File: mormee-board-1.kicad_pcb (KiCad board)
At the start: 2 copper layers, 1 part, among them U1 RTL8735BDM-A20-N04

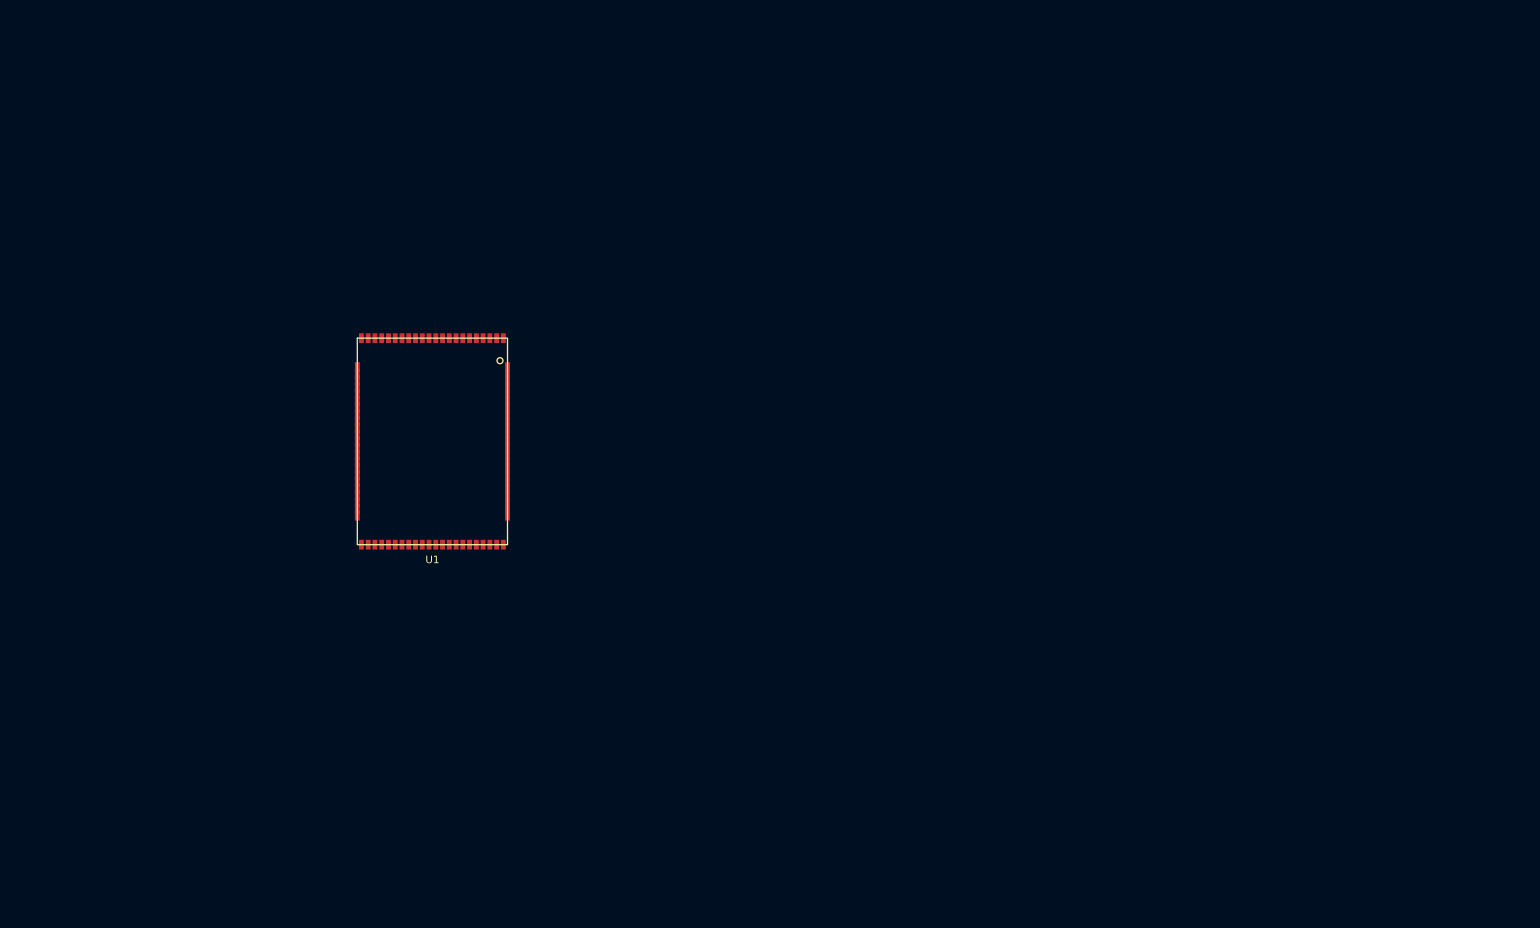
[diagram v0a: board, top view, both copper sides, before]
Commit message: All footprints configured correctly. Next step is layout
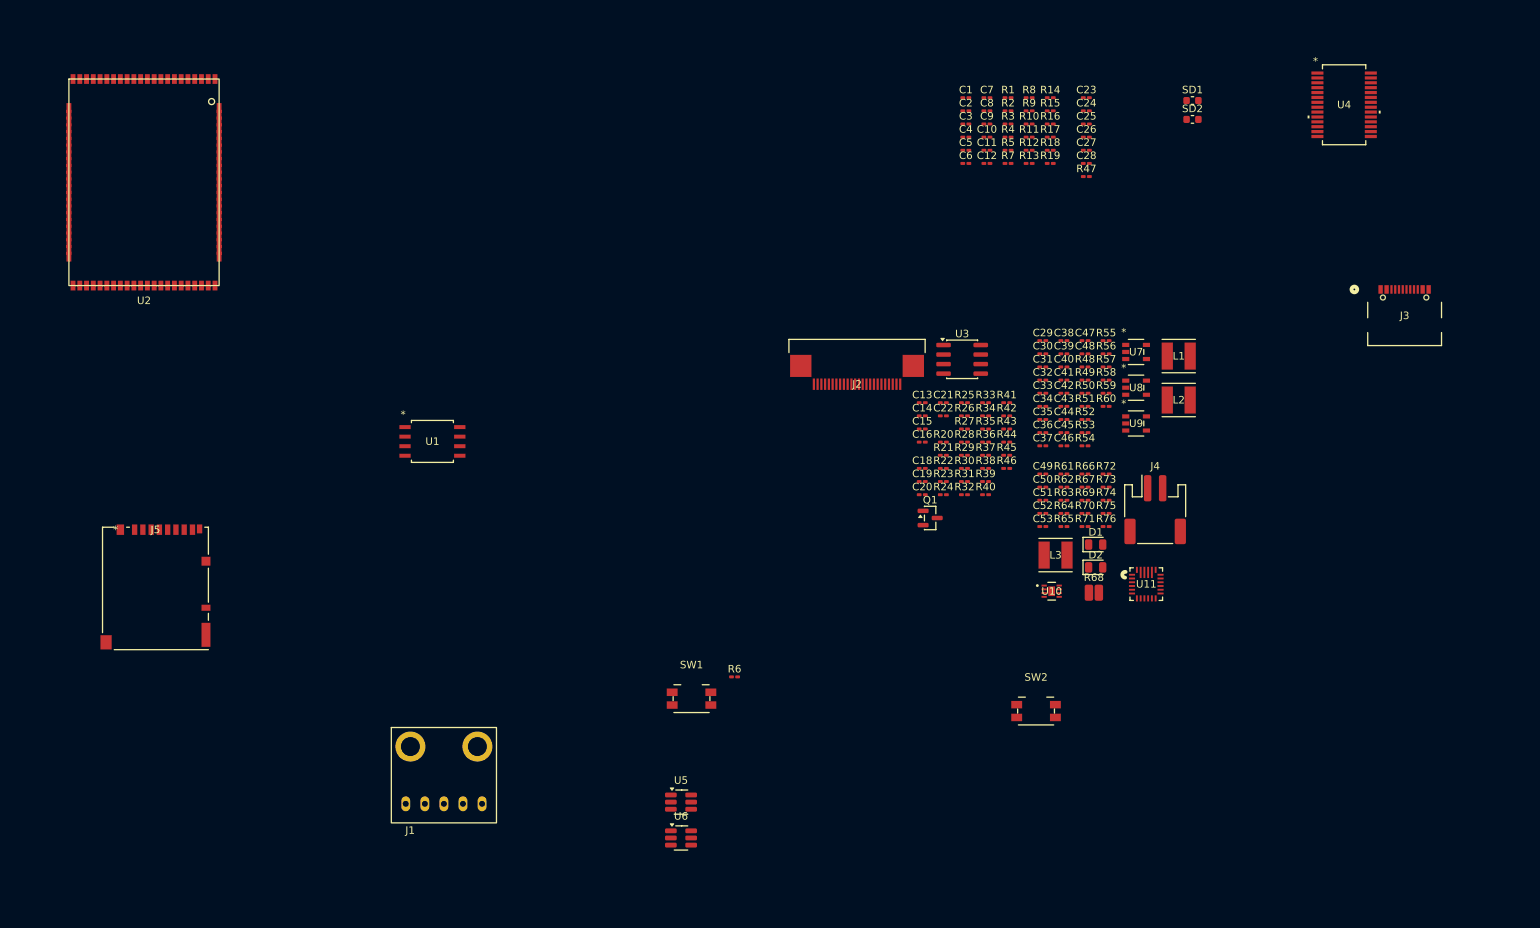
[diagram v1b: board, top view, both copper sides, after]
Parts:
- added C1: 0.1uF/10V, Capacitor_SMD:C_0201_0603Metric_Pad0.64x0.40mm_HandSolder, F.Cu at (193.6, 32.5)
- added C10: 4.7uF/10V, Capacitor_SMD:C_0201_0603Metric_Pad0.64x0.40mm_HandSolder, F.Cu at (196.4, 37.7)
- added C11: 0.1uF/10V, Capacitor_SMD:C_0201_0603Metric_Pad0.64x0.40mm_HandSolder, F.Cu at (196.4, 39.5)
- added C12: 10uF/10V, Capacitor_SMD:C_0201_0603Metric_Pad0.64x0.40mm_HandSolder, F.Cu at (196.4, 41.2)
- added C13: 0.1uF/10V, Capacitor_SMD:C_0201_0603Metric_Pad0.64x0.40mm_HandSolder, F.Cu at (187.8, 73.1)
- added C14: 2.2uF/10V, Capacitor_SMD:C_0201_0603Metric_Pad0.64x0.40mm_HandSolder, F.Cu at (187.8, 74.8)
- added C15: 10uF/10V, Capacitor_SMD:C_0201_0603Metric_Pad0.64x0.40mm_HandSolder, F.Cu at (187.8, 76.6)
- added C16: 0.1uF/10V, Capacitor_SMD:C_0201_0603Metric_Pad0.64x0.40mm_HandSolder, F.Cu at (187.8, 78.3)
- added C18: 0.1uF/10V, Capacitor_SMD:C_0201_0603Metric_Pad0.64x0.40mm_HandSolder, F.Cu at (187.8, 81.8)
- added C19: 0.1uF/10V, Capacitor_SMD:C_0201_0603Metric_Pad0.64x0.40mm_HandSolder, F.Cu at (187.8, 83.6)
- added C2: 0.1uF/10V, Capacitor_SMD:C_0201_0603Metric_Pad0.64x0.40mm_HandSolder, F.Cu at (193.6, 34.2)
- added C20: 0.1uF/10V, Capacitor_SMD:C_0201_0603Metric_Pad0.64x0.40mm_HandSolder, F.Cu at (187.8, 85.3)
- added C21: 0.1uF/10V/NC, Capacitor_SMD:C_0201_0603Metric_Pad0.64x0.40mm_HandSolder, F.Cu at (190.6, 73.1)
- added C22: 0.1uF/10V, Capacitor_SMD:C_0201_0603Metric_Pad0.64x0.40mm_HandSolder, F.Cu at (190.6, 74.8)
- added C23: 0.1uF/10V, Capacitor_SMD:C_0201_0603Metric_Pad0.64x0.40mm_HandSolder, F.Cu at (209.6, 32.5)
- added C24: 2.2uF/10V, Capacitor_SMD:C_0201_0603Metric_Pad0.64x0.40mm_HandSolder, F.Cu at (209.6, 34.2)
- added C25: 0.1uF, Capacitor_SMD:C_0201_0603Metric_Pad0.64x0.40mm_HandSolder, F.Cu at (209.6, 36.0)
- added C26: 0.1uF, Capacitor_SMD:C_0201_0603Metric_Pad0.64x0.40mm_HandSolder, F.Cu at (209.6, 37.7)
- added C27: 0.1uF, Capacitor_SMD:C_0201_0603Metric_Pad0.64x0.40mm_HandSolder, F.Cu at (209.6, 39.5)
- added C28: 4.7uF, Capacitor_SMD:C_0201_0603Metric_Pad0.64x0.40mm_HandSolder, F.Cu at (209.6, 41.2)
- added C29: 0.1uF/10V, Capacitor_SMD:C_0201_0603Metric_Pad0.64x0.40mm_HandSolder, F.Cu at (203.8, 64.8)
- added C3: 10uF/10V, Capacitor_SMD:C_0201_0603Metric_Pad0.64x0.40mm_HandSolder, F.Cu at (193.6, 36.0)
- added C30: 0.1uF/10V, Capacitor_SMD:C_0201_0603Metric_Pad0.64x0.40mm_HandSolder, F.Cu at (203.8, 66.6)
- added C31: 10uF/10V, Capacitor_SMD:C_0201_0603Metric_Pad0.64x0.40mm_HandSolder, F.Cu at (203.8, 68.3)
- added C32: 10uF/10V, Capacitor_SMD:C_0201_0603Metric_Pad0.64x0.40mm_HandSolder, F.Cu at (203.8, 70.1)
- added C33: 68pF, Capacitor_SMD:C_0201_0603Metric_Pad0.64x0.40mm_HandSolder, F.Cu at (203.8, 71.8)
- added C34: 10uF/10V, Capacitor_SMD:C_0201_0603Metric_Pad0.64x0.40mm_HandSolder, F.Cu at (203.8, 73.6)
- added C35: 10uF/10V, Capacitor_SMD:C_0201_0603Metric_Pad0.64x0.40mm_HandSolder, F.Cu at (203.8, 75.3)
- added C36: 0.1uF/10V, Capacitor_SMD:C_0201_0603Metric_Pad0.64x0.40mm_HandSolder, F.Cu at (203.8, 77.1)
- added C37: 0.1uF/10V, Capacitor_SMD:C_0201_0603Metric_Pad0.64x0.40mm_HandSolder, F.Cu at (203.8, 78.8)
- added C38: 2.2uF/10V, Capacitor_SMD:C_0201_0603Metric_Pad0.64x0.40mm_HandSolder, F.Cu at (206.6, 64.8)
- added C39: 2.2uF/10V, Capacitor_SMD:C_0201_0603Metric_Pad0.64x0.40mm_HandSolder, F.Cu at (206.6, 66.6)
- added C4: 10uF/10V, Capacitor_SMD:C_0201_0603Metric_Pad0.64x0.40mm_HandSolder, F.Cu at (193.6, 37.7)
- added C40: 2.2uF/10V, Capacitor_SMD:C_0201_0603Metric_Pad0.64x0.40mm_HandSolder, F.Cu at (206.6, 68.3)
- added C41: 2.2uF/10V, Capacitor_SMD:C_0201_0603Metric_Pad0.64x0.40mm_HandSolder, F.Cu at (206.6, 70.1)
- added C42: 2.2uF/10V, Capacitor_SMD:C_0201_0603Metric_Pad0.64x0.40mm_HandSolder, F.Cu at (206.6, 71.8)
- added C43: 2.2uF/10V, Capacitor_SMD:C_0201_0603Metric_Pad0.64x0.40mm_HandSolder, F.Cu at (206.6, 73.6)
- added C44: 2.2uF/10V, Capacitor_SMD:C_0201_0603Metric_Pad0.64x0.40mm_HandSolder, F.Cu at (206.6, 75.3)
- added C45: 2.2uF/10V, Capacitor_SMD:C_0201_0603Metric_Pad0.64x0.40mm_HandSolder, F.Cu at (206.6, 77.1)
- added C46: 2.2uF/10V, Capacitor_SMD:C_0201_0603Metric_Pad0.64x0.40mm_HandSolder, F.Cu at (206.6, 78.8)
- added C47: 2.2uF/10V, Capacitor_SMD:C_0201_0603Metric_Pad0.64x0.40mm_HandSolder, F.Cu at (209.4, 64.8)
- added C48: 2.2uF/10V, Capacitor_SMD:C_0201_0603Metric_Pad0.64x0.40mm_HandSolder, F.Cu at (209.4, 66.6)
- added C49: 120pF, Capacitor_SMD:C_0201_0603Metric_Pad0.64x0.40mm_HandSolder, F.Cu at (203.8, 82.6)
- added C5: 22uF6.3V, Capacitor_SMD:C_0201_0603Metric_Pad0.64x0.40mm_HandSolder, F.Cu at (193.6, 39.5)
- added C50: 0.1uF, Capacitor_SMD:C_0201_0603Metric_Pad0.64x0.40mm_HandSolder, F.Cu at (203.8, 84.3)
- added C51: 100nF, Capacitor_SMD:C_0201_0603Metric_Pad0.64x0.40mm_HandSolder, F.Cu at (203.8, 86.1)
- added C52: 10uF, Capacitor_SMD:C_0201_0603Metric_Pad0.64x0.40mm_HandSolder, F.Cu at (203.8, 87.8)
- added C53: 100nF, Capacitor_SMD:C_0201_0603Metric_Pad0.64x0.40mm_HandSolder, F.Cu at (203.8, 89.6)
- added C6: 0.1uF/10V, Capacitor_SMD:C_0201_0603Metric_Pad0.64x0.40mm_HandSolder, F.Cu at (193.6, 41.2)
- added C7: 10pF/NC, Capacitor_SMD:C_0201_0603Metric_Pad0.64x0.40mm_HandSolder, F.Cu at (196.4, 32.5)
- added C8: 10uF/10V, Capacitor_SMD:C_0201_0603Metric_Pad0.64x0.40mm_HandSolder, F.Cu at (196.4, 34.2)
- added C9: 0.1uF/10V, Capacitor_SMD:C_0201_0603Metric_Pad0.64x0.40mm_HandSolder, F.Cu at (196.4, 36.0)
- added D1: RED, LED_SMD:LED_0805_2012Metric, F.Cu at (210.9, 92.0)
- added D2: BLUE, LED_SMD:LED_0805_2012Metric, F.Cu at (210.9, 95.0)
- added J1: PDM MEMS Mic, Adafruit:Adafruit MEMS 3492, F.Cu at (117.1, 116.3)
- added J2: 24FLZ-SM2-TB, JST 24FLZ-SM2-TB:CON24_1X24_DB_JST, F.Cu at (179.1, 68.1)
- added J3: USB4105-GF-A, USB4105-GF-A:USB4105_GCT, F.Cu at (252.0, 61.5)
- added J4: Conn_01x02, Connector_JST:JST_PH_S2B-PH-SM4-TB_1x02-1MP_P2.00mm_Horizontal, F.Cu at (218.8, 87.3)
- added J5: DM3BT-DSF-PEJS, DM3BT-DSF-PEJS:DM3BT-DSF-PEJS_HIR, F.Cu at (85.7, 97.8)
- added L1: SRN4018-2R2M, SRN4018-2R2M:IND_BOURNS_SRN4018, F.Cu at (221.9, 66.9)
- added L2: SRN4018-2R2M, SRN4018-2R2M:IND_BOURNS_SRN4018, F.Cu at (221.9, 72.7)
- added L3: SRN4018-2R2M, SRN4018-2R2M:IND_BOURNS_SRN4018, F.Cu at (205.5, 93.4)
- added Q1: AO3401A, Package_TO_SOT_SMD:SOT-23, F.Cu at (188.8, 88.4)
- added R1: 10K, Resistor_SMD:R_0201_0603Metric_Pad0.64x0.40mm_HandSolder, F.Cu at (199.2, 32.5)
- added R10: 0, Resistor_SMD:R_0201_0603Metric_Pad0.64x0.40mm_HandSolder, F.Cu at (202.0, 36.0)
- added R11: 0, Resistor_SMD:R_0201_0603Metric_Pad0.64x0.40mm_HandSolder, F.Cu at (202.0, 37.7)
- added R12: 10K, Resistor_SMD:R_0201_0603Metric_Pad0.64x0.40mm_HandSolder, F.Cu at (202.0, 39.5)
- added R13: 10K, Resistor_SMD:R_0201_0603Metric_Pad0.64x0.40mm_HandSolder, F.Cu at (202.0, 41.2)
- added R14: 10K, Resistor_SMD:R_0201_0603Metric_Pad0.64x0.40mm_HandSolder, F.Cu at (204.8, 32.5)
- added R15: 10K, Resistor_SMD:R_0201_0603Metric_Pad0.64x0.40mm_HandSolder, F.Cu at (204.8, 34.2)
- added R16: 10K, Resistor_SMD:R_0201_0603Metric_Pad0.64x0.40mm_HandSolder, F.Cu at (204.8, 36.0)
- added R17: 10K, Resistor_SMD:R_0201_0603Metric_Pad0.64x0.40mm_HandSolder, F.Cu at (204.8, 37.7)
- added R18: 0, Resistor_SMD:R_0201_0603Metric_Pad0.64x0.40mm_HandSolder, F.Cu at (204.8, 39.5)
- added R19: 1K, Resistor_SMD:R_0201_0603Metric_Pad0.64x0.40mm_HandSolder, F.Cu at (204.8, 41.2)
- added R2: 10K, Resistor_SMD:R_0201_0603Metric_Pad0.64x0.40mm_HandSolder, F.Cu at (199.2, 34.2)
- added R20: 0, Resistor_SMD:R_0201_0603Metric_Pad0.64x0.40mm_HandSolder, F.Cu at (190.6, 78.3)
- added R21: 10K, Resistor_SMD:R_0201_0603Metric_Pad0.64x0.40mm_HandSolder, F.Cu at (190.6, 80.1)
- added R22: 33K, Resistor_SMD:R_0201_0603Metric_Pad0.64x0.40mm_HandSolder, F.Cu at (190.6, 81.8)
- added R23: 33K, Resistor_SMD:R_0201_0603Metric_Pad0.64x0.40mm_HandSolder, F.Cu at (190.6, 83.6)
- added R24: 33K, Resistor_SMD:R_0201_0603Metric_Pad0.64x0.40mm_HandSolder, F.Cu at (190.6, 85.3)
- added R25: 0, Resistor_SMD:R_0201_0603Metric_Pad0.64x0.40mm_HandSolder, F.Cu at (193.4, 73.1)
- added R26: 33K, Resistor_SMD:R_0201_0603Metric_Pad0.64x0.40mm_HandSolder, F.Cu at (193.4, 74.8)
- added R27: 33K, Resistor_SMD:R_0201_0603Metric_Pad0.64x0.40mm_HandSolder, F.Cu at (193.4, 76.6)
- added R28: 33K, Resistor_SMD:R_0201_0603Metric_Pad0.64x0.40mm_HandSolder, F.Cu at (193.4, 78.3)
- added R29: 33K, Resistor_SMD:R_0201_0603Metric_Pad0.64x0.40mm_HandSolder, F.Cu at (193.4, 80.1)
- added R3: 0, Resistor_SMD:R_0201_0603Metric_Pad0.64x0.40mm_HandSolder, F.Cu at (199.2, 36.0)
- added R30: 0, Resistor_SMD:R_0201_0603Metric_Pad0.64x0.40mm_HandSolder, F.Cu at (193.4, 81.8)
- added R31: 47K, Resistor_SMD:R_0201_0603Metric_Pad0.64x0.40mm_HandSolder, F.Cu at (193.4, 83.6)
- added R32: 47K, Resistor_SMD:R_0201_0603Metric_Pad0.64x0.40mm_HandSolder, F.Cu at (193.4, 85.3)
- added R33: 47K, Resistor_SMD:R_0201_0603Metric_Pad0.64x0.40mm_HandSolder, F.Cu at (196.2, 73.1)
- added R34: 47K, Resistor_SMD:R_0201_0603Metric_Pad0.64x0.40mm_HandSolder, F.Cu at (196.2, 74.8)
- added R35: 47K, Resistor_SMD:R_0201_0603Metric_Pad0.64x0.40mm_HandSolder, F.Cu at (196.2, 76.6)
- added R36: 10K, Resistor_SMD:R_0201_0603Metric_Pad0.64x0.40mm_HandSolder, F.Cu at (196.2, 78.3)
- added R37: 4.7K, Resistor_SMD:R_0201_0603Metric_Pad0.64x0.40mm_HandSolder, F.Cu at (196.2, 80.1)
- added R38: 4.7K, Resistor_SMD:R_0201_0603Metric_Pad0.64x0.40mm_HandSolder, F.Cu at (196.2, 81.8)
- added R39: 470, Resistor_SMD:R_0201_0603Metric_Pad0.64x0.40mm_HandSolder, F.Cu at (196.2, 83.6)
- added R4: 0, Resistor_SMD:R_0201_0603Metric_Pad0.64x0.40mm_HandSolder, F.Cu at (199.2, 37.7)
- added R40: 5.6K, Resistor_SMD:R_0201_0603Metric_Pad0.64x0.40mm_HandSolder, F.Cu at (196.2, 85.3)
- added R41: 5.6K, Resistor_SMD:R_0201_0603Metric_Pad0.64x0.40mm_HandSolder, F.Cu at (199.0, 73.1)
- added R42: 560, Resistor_SMD:R_0201_0603Metric_Pad0.64x0.40mm_HandSolder, F.Cu at (199.0, 74.8)
- added R43: 4.7K, Resistor_SMD:R_0201_0603Metric_Pad0.64x0.40mm_HandSolder, F.Cu at (199.0, 76.6)
- added R44: 4.7K, Resistor_SMD:R_0201_0603Metric_Pad0.64x0.40mm_HandSolder, F.Cu at (199.0, 78.3)
- added R45: 10K, Resistor_SMD:R_0201_0603Metric_Pad0.64x0.40mm_HandSolder, F.Cu at (199.0, 80.1)
- added R46: 10K, Resistor_SMD:R_0201_0603Metric_Pad0.64x0.40mm_HandSolder, F.Cu at (199.0, 81.8)
- added R47: 10K, Resistor_SMD:R_0201_0603Metric_Pad0.64x0.40mm_HandSolder, F.Cu at (209.6, 43.0)
- added R48: 10K, Resistor_SMD:R_0201_0603Metric_Pad0.64x0.40mm_HandSolder, F.Cu at (209.4, 68.3)
- added R49: 100K, Resistor_SMD:R_0201_0603Metric_Pad0.64x0.40mm_HandSolder, F.Cu at (209.4, 70.1)
- added R5: 0, Resistor_SMD:R_0201_0603Metric_Pad0.64x0.40mm_HandSolder, F.Cu at (199.2, 39.5)
- added R50: 100K, Resistor_SMD:R_0201_0603Metric_Pad0.64x0.40mm_HandSolder, F.Cu at (209.4, 71.8)
- added R51: 200K/1%, Resistor_SMD:R_0201_0603Metric_Pad0.64x0.40mm_HandSolder, F.Cu at (209.4, 73.6)
- added R52: 0, Resistor_SMD:R_0201_0603Metric_Pad0.64x0.40mm_HandSolder, F.Cu at (209.4, 75.3)
- added R53: 0, Resistor_SMD:R_0201_0603Metric_Pad0.64x0.40mm_HandSolder, F.Cu at (209.4, 77.1)
- added R54: 150K/1%, Resistor_SMD:R_0201_0603Metric_Pad0.64x0.40mm_HandSolder, F.Cu at (209.4, 78.8)
- added R55: 44.2K/1%, Resistor_SMD:R_0201_0603Metric_Pad0.64x0.40mm_HandSolder, F.Cu at (212.3, 64.8)
- added R56: 120K/1%, Resistor_SMD:R_0201_0603Metric_Pad0.64x0.40mm_HandSolder, F.Cu at (212.3, 66.6)
- added R57: 200K/1%, Resistor_SMD:R_0201_0603Metric_Pad0.64x0.40mm_HandSolder, F.Cu at (212.3, 68.3)
- added R58: 47K, Resistor_SMD:R_0201_0603Metric_Pad0.64x0.40mm_HandSolder, F.Cu at (212.3, 70.1)
- added R59: 47K, Resistor_SMD:R_0201_0603Metric_Pad0.64x0.40mm_HandSolder, F.Cu at (212.3, 71.8)
- added R6: 0, Resistor_SMD:R_0201_0603Metric_Pad0.64x0.40mm_HandSolder, F.Cu at (162.8, 109.6)
- added R60: 47K, Resistor_SMD:R_0201_0603Metric_Pad0.64x0.40mm_HandSolder, F.Cu at (212.3, 73.6)
- added R61: 15K, Resistor_SMD:R_0201_0603Metric_Pad0.64x0.40mm_HandSolder, F.Cu at (206.6, 82.6)
- added R62: 5.1K, Resistor_SMD:R_0201_0603Metric_Pad0.64x0.40mm_HandSolder, F.Cu at (206.6, 84.3)
- added R63: 2.1K, Resistor_SMD:R_0201_0603Metric_Pad0.64x0.40mm_HandSolder, F.Cu at (206.6, 86.1)
- added R64: 2.1K, Resistor_SMD:R_0201_0603Metric_Pad0.64x0.40mm_HandSolder, F.Cu at (206.6, 87.8)
- added R65: 31.6K, Resistor_SMD:R_0201_0603Metric_Pad0.64x0.40mm_HandSolder, F.Cu at (206.6, 89.6)
- added R66: 10K, Resistor_SMD:R_0201_0603Metric_Pad0.64x0.40mm_HandSolder, F.Cu at (209.4, 82.6)
- added R67: 147K, Resistor_SMD:R_0201_0603Metric_Pad0.64x0.40mm_HandSolder, F.Cu at (209.4, 84.3)
- added R68: 20m, Resistor_SMD:R_0508_1220Metric_Pad1.12x2.15mm_HandSolder, F.Cu at (210.6, 98.4)
- added R69: 147K, Resistor_SMD:R_0201_0603Metric_Pad0.64x0.40mm_HandSolder, F.Cu at (209.4, 86.1)
- added R7: 0, Resistor_SMD:R_0201_0603Metric_Pad0.64x0.40mm_HandSolder, F.Cu at (199.2, 41.2)
- added R70: 10K, Resistor_SMD:R_0201_0603Metric_Pad0.64x0.40mm_HandSolder, F.Cu at (209.4, 87.8)
- added R71: 10K, Resistor_SMD:R_0201_0603Metric_Pad0.64x0.40mm_HandSolder, F.Cu at (209.4, 89.6)
- added R72: 90K, Resistor_SMD:R_0201_0603Metric_Pad0.64x0.40mm_HandSolder, F.Cu at (212.3, 82.6)
- added R73: 2.1K, Resistor_SMD:R_0201_0603Metric_Pad0.64x0.40mm_HandSolder, F.Cu at (212.3, 84.3)
- added R74: 2.1K, Resistor_SMD:R_0201_0603Metric_Pad0.64x0.40mm_HandSolder, F.Cu at (212.3, 86.1)
- added R75: 23.7K, Resistor_SMD:R_0201_0603Metric_Pad0.64x0.40mm_HandSolder, F.Cu at (212.3, 87.8)
- added R76: 5.1K, Resistor_SMD:R_0201_0603Metric_Pad0.64x0.40mm_HandSolder, F.Cu at (212.3, 89.6)
- added R8: 0, Resistor_SMD:R_0201_0603Metric_Pad0.64x0.40mm_HandSolder, F.Cu at (202.0, 32.5)
- added R9: 10K, Resistor_SMD:R_0201_0603Metric_Pad0.64x0.40mm_HandSolder, F.Cu at (202.0, 34.2)
- added SD1: PGB1010603MRHF/NC, Fuse:Fuse_0603_1608Metric, F.Cu at (223.8, 32.9)
- added SD2: PGB1010603MRHF/NC, Fuse:Fuse_0603_1608Metric, F.Cu at (223.8, 35.4)
- added SW1: EVQ-PUB02K, Button_Switch_SMD:Panasonic_EVQPUK_EVQPUB, F.Cu at (157.1, 112.5)
- added SW2: EVQ-PUB02K, Button_Switch_SMD:Panasonic_EVQPUK_EVQPUB, F.Cu at (202.9, 114.2)
- added U10: MAX17048G+T10, MAX17048G-T10:21-0168E_T822-3_MXM, F.Cu at (205.0, 98.2)
- added U11: MP2637GR-P, MP2637:QFN-24_MP2637_MNP, F.Cu at (217.6, 97.2)
- added U2: RTL8735BDM-A20-N04, RTL8735BDM-A20-N04:RTL8735BDM-A20-N04, F.Cu at (84.2, 43.8)
- added U3: FDS9926A, Package_SO:SOIC-8_3.9x4.9mm_P1.27mm, F.Cu at (193.1, 67.3)
- added U4: FT232RNL-REEL, FT232RNL:SSOP-28_FTD, F.Cu at (243.9, 33.4)
- added U5: RT8097AHGE, Package_TO_SOT_SMD:SOT-23-6_Handsoldering, F.Cu at (155.7, 126.3)
- added U6: RT8097AHGE, Package_TO_SOT_SMD:SOT-23-6_Handsoldering, F.Cu at (155.7, 131.1)
- added U7: RT9080-28GJ5, RTL9080:TSOT-23-5_RIT, F.Cu at (216.2, 66.3)
- added U8: RT9080-18GJ5, RTL9080:TSOT-23-5_RIT, F.Cu at (216.2, 71.1)
- added U9: RT9080-12GJ5, RTL9080:TSOT-23-5_RIT, F.Cu at (216.2, 75.9)
- U1: value RTL8735BDM-A20-N04 -> W25Q128JVSIQ; footprint RTL8735BDM-A20-N04:RTL8735BDM-A20-N04 -> W25Q128JVSIQ:SOIC_128JVSIQ_WIN
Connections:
- U1 pad 1: unconnected-(U1-FLASH_D3-Pad1) -> /RTL9835B/FLASH_CS
- U1 pad 2: unconnected-(U1-FLASH_D1-Pad2) -> /RTL9835B/FLASH_D1
- U1 pad 3: unconnected-(U1-SD_D1-Pad3) -> /RTL9835B/FLASH_D2
- U1 pad 4: unconnected-(U1-SD_D0-Pad4) -> GND
- U1 pad 5: unconnected-(U1-SD_CMD-Pad5) -> /RTL9835B/FLASH_D0
- U1 pad 6: unconnected-(U1-SD_D3-Pad6) -> /RTL9835B/FLASH_CLK
- U1 pad 7: unconnected-(U1-SD_D2-Pad7) -> /RTL9835B/FLASH_D3
- U1 pad 8: unconnected-(U1-SD_CD-Pad8) -> SOC_FLASH
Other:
- copper layers 2 -> 4

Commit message: In the middle of layout. WIP
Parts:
- removed R20, R25, R30: 0, Resistor_SMD:R_0201_0603Metric_Pad0.64x0.40mm_HandSolder
- added TP1: +3.3V_TP, TestPoint:TestPoint_Pad_D1.5mm, F.Cu at (140.5, 48.0)
- added TP2: +2.8V_TP, TestPoint:TestPoint_Pad_D1.5mm, F.Cu at (140.5, 54.0)
- added TP3: +1.8V_TP, TestPoint:TestPoint_Pad_D1.5mm, F.Cu at (140.5, 59.5)
- added TP4: VDD_DDR_TP, TestPoint:TestPoint_Pad_D1.5mm, F.Cu at (150.5, 48.0)
- added TP5: +1.2V_TP, TestPoint:TestPoint_Pad_D1.5mm, F.Cu at (150.5, 54.0)
- added TP6: SD_3.3V_TP, TestPoint:TestPoint_Pad_D1.5mm, F.Cu at (150.5, 59.5)
- added TP7: V_USB_TP, TestPoint:TestPoint_Pad_D1.5mm, F.Cu at (160.0, 48.0)
- added TP8: V_BATT_TP, TestPoint:TestPoint_Pad_D1.5mm, F.Cu at (160.0, 54.0)
- added TP9: GND_TP, TestPoint:TestPoint_Pad_D1.5mm, F.Cu at (160.0, 59.5)
- C1, C11, C13, C16, C18, C19, C2, C20, C22, C23, C29, C30, C36, C37, C6, C9: value 0.1uF/10V -> 0.1uF
- C10: value 4.7uF/10V -> 4.7uF
- C12, C15, C3, C31, C32, C34, C35, C4, C8: value 10uF/10V -> 10uF
- C14, C24, C38, C39, C40, C41, C42, C43, C44, C45, C46, C47, C48: value 2.2uF/10V -> 2.2uF
- C21: value 0.1uF/10V/NC -> 0.1uF/NC
- C5: value 22uF6.3V -> 22uF
- J4, U2: moved to B.Cu
- moved J4 127.6 mm to (91.5, 78.0), turned to -90 degrees
- moved R33 115.8 mm to (81.0, 84.5)
- moved R34 113.2 mm to (83.4, 84.5), turned to 180 degrees
- moved R35 110.9 mm to (85.6, 84.5), turned to 180 degrees
- moved R22 108.2 mm to (82.5, 87.6)
- moved R23 107.1 mm to (83.5, 86.5)
- moved R26 106.3 mm to (88.0, 88.5), turned to 180 degrees
- moved R21 106.1 mm to (84.4, 79.5), turned to -90 degrees
- moved R24 105.5 mm to (85.1, 87.6)
- moved C15 104.9 mm to (82.9, 81.5), turned to 90 degrees
- moved R27 104.9 mm to (89.0, 86.5)
- moved C16 104.8 mm to (82.9, 79.5), turned to 90 degrees
- moved R31 104.4 mm to (89.0, 84.5), turned to 180 degrees
- moved R28 103.3 mm to (90.5, 87.7), turned to 180 degrees
- moved R36 102.5 mm to (94.0, 86.5), turned to 180 degrees
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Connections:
- J5 pad 4: Net-(J5-VDD) -> SD_3V3
- Q1 pad 2: Net-(Q1-S) -> +3.3V
- R29 pad 1: unconnected-(R29-Pad1) -> +3.3V
- R31 pad 1: Net-(R30-Pad2) -> VDIO_SD
- R32 pad 1: Net-(R30-Pad2) -> VDIO_SD
- R33 pad 1: Net-(R30-Pad2) -> VDIO_SD
- R34 pad 1: Net-(R30-Pad2) -> VDIO_SD
- R35 pad 1: Net-(R30-Pad2) -> VDIO_SD
- R36 pad 1: Net-(R30-Pad2) -> VDIO_SD
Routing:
- net /Battery/VCC: track 0.00 -> 32.5 mm, vias 0 -> 2
- net Net-(U11-*CHG): track 0.00 -> 12.0 mm, vias 0 -> 2
- net Net-(U11-CSP): track 0.00 -> 10.9 mm
- net V_USB: track 0.00 -> 10.9 mm, vias 0 -> 2
- net SD_3V3: track 0.00 -> 9.95 mm
- net V_BATT: track 0.00 -> 7.50 mm
- net Net-(U11-SW): track 0.00 -> 7.03 mm
- net Net-(U11-FB): track 0.00 -> 6.71 mm
- net Net-(U11-*ACOK): track 0.00 -> 5.83 mm
- net Net-(U11-REG): track 0.00 -> 5.75 mm
- net Net-(U11-PWIN): track 0.00 -> 4.72 mm
- net Net-(U11-NTC): track 0.00 -> 4.52 mm
- net SD_CD: track 0.00 -> 4.25 mm
- net +5V: track 0.00 -> 4.20 mm
- net Net-(U11-ISET): track 0.00 -> 4.09 mm
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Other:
- board outline added: 201 x 119.5 mm

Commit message: Breakthrough in PCB layout. WIP
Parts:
- removed C34, C35: 10uF, Capacitor_SMD:C_0201_0603Metric_Pad0.64x0.40mm_HandSolder
- removed R10, R11, R18, R3, R4, R5, R52, R53, R6, R7, R8: 0, Resistor_SMD:R_0201_0603Metric_Pad0.64x0.40mm_HandSolder
- C11, C12, C13, C14, C15, C16, C23, C24, C5, C6, C8, L1, L2, Q1, R12, R13, R14, R15, R16, R17, R21, R22, R23, R24, R26, R27, R28, R29, R31, R32, R33, R34, R35, R36, SD1, SD2: moved to B.Cu
- moved L1 147.5 mm to (74.7, 76.2), turned to 180 degrees
- moved J3 147.1 mm to (105.0, 65.5), turned to 90 degrees
- moved U4 143.9 mm to (101.5, 54.0)
- moved SW2 141.3 mm to (73.0, 58.5), turned to 90 degrees
- moved L2 136.6 mm to (85.4, 76.0), turned to 180 degrees
- moved R55 134.9 mm to (78.1, 79.2)
- moved R19 134.8 mm to (73.4, 71.0), turned to 180 degrees
- moved R51 133.5 mm to (76.1, 79.2)
- moved R50 131.2 mm to (78.3, 76.3)
- moved C31 130.3 mm to (74.0, 79.2), turned to 180 degrees
- moved C38 129.1 mm to (78.3, 78.4)
- moved U8 128.0 mm to (89.4, 54.2), turned to 180 degrees
- moved U9 127.4 mm to (89.2, 66.3), turned to 180 degrees
- moved U7 127.0 mm to (89.4, 60.3), turned to 180 degrees
- moved R2 125.9 mm to (77.9, 68.2), turned to 180 degrees
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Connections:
- net Net-(U11-CSP) renamed /Battery/L3
- net Net-(U11-SW) renamed /Battery/SW
- net Net-(U5-LX) renamed /Power/L1
- net Net-(U6-LX) renamed /Power/L2
- C10 pad 1: SOC_FLASH -> +3.3V
- C31 pad 1: Net-(C31-Pad1) -> +3.3V
- C32 pad 1: Net-(C32-Pad1) -> VDD_DDR
- C33 pad 2: Net-(C32-Pad1) -> VDD_DDR
- C9 pad 1: SOC_FLASH -> +3.3V
- J1 pad 4: /SD CARD /Vidio / Audio / USB/DMIC_CLK -> DMIC_CLK
- J1 pad 5: /SD CARD /Vidio / Audio / USB/DMIC_DATA -> DMIC_DATA
- L1 pad 1: Net-(C31-Pad1) -> +3.3V
- L2 pad 1: Net-(C32-Pad1) -> VDD_DDR
- R1 pad 1: SOC_FLASH -> +3.3V
- R12 pad 2: /RTL9835B/LOG_IN -> CH_UART_TX
- R13 pad 2: /RTL9835B/LOG_OUT -> CH_UART_RX
- R2 pad 1: SOC_FLASH -> +3.3V
- R51 pad 1: Net-(C31-Pad1) -> +3.3V
- R54 pad 1: Net-(C32-Pad1) -> VDD_DDR
- R9 pad 1: SOC_FLASH -> +3.3V
- U1 pad 8: SOC_FLASH -> +3.3V
- U2 pad 1: Net-(U2-FLASH_D3) -> /RTL9835B/FLASH_D3
- U2 pad 2: Net-(U2-FLASH_D1) -> /RTL9835B/FLASH_D1
- U2 pad 31: /RTL9835B/DMIC_CLK -> DMIC_CLK
- U2 pad 35: /RTL9835B/DMIC_DATA -> DMIC_DATA
- U2 pad 48: Net-(U2-UART1_IN) -> CH_UART_TX
- U2 pad 49: Net-(U2-UART1_OUT) -> CH_UART_RX
- U2 pad 77: Net-(U2-MIC1_P) -> /RTL9835B/MIC1_P
- U2 pad 88: Net-(U2-FLASH_D0) -> /RTL9835B/FLASH_D0
- U2 pad 89: Net-(U2-FLASH_D2) -> /RTL9835B/FLASH_D2
- U2 pad 90: Net-(U2-FLASH_CS) -> /RTL9835B/FLASH_CS
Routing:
- net GND: track 0.00 -> 103.7 mm, vias 0 -> 61
- net SD_CLK: track 0.00 -> 43.1 mm, vias 0 -> 2
- net SEN_1V2: track 0.00 -> 34.8 mm
- net +3.3V: track 3.58 -> 37.9 mm, vias 0 -> 9
- net SEN_1V8: track 0.00 -> 31.7 mm
- net SEN_2V8: track 0.00 -> 28.5 mm
- net /SD CARD /Vidio / Audio / USB/SDA: track 0.00 -> 23.5 mm, vias 0 -> 2
- net /SD CARD /Vidio / Audio / USB/SCL: track 0.00 -> 22.5 mm, vias 0 -> 2
- net MDN2: track 0.00 -> 20.6 mm, vias 0 -> 1
- net /Debug Interface/USB_N: track 0.00 -> 18.1 mm, vias 0 -> 1
- net VDD_DDR: track 0.00 -> 16.8 mm, vias 0 -> 2
- net MDP1: track 0.00 -> 15.5 mm, vias 0 -> 1
- net /RTL9835B/FLASH_CLK: track 0.00 -> 14.8 mm, vias 0 -> 1
- net MDN1: track 0.00 -> 14.8 mm, vias 0 -> 1
- net MDP3: track 0.00 -> 14.1 mm, vias 0 -> 1
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- added copper zone on In2.Cu, net +3.3V
- added copper zone on In2.Cu, net +5V
- added copper zone on In1.Cu, net GND
- added copper zone on In2.Cu, net V_USB
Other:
- board size 201 x 119.5 mm -> 40 x 60 mm
